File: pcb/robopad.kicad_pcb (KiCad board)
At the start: 2 copper layers, 100 x 100 mm, 34 parts, among them IC1 Left Slider, IC2 Right Slider, SW1 SW_Push, SW2 SW_Push, SW3 SW_Push, SW4 SW_Push, SW5 SW_Push, SW6 SW_Push, SW7 SW_Push, SW8 SW_Push, SW9 SW_Push, U1 XIAO-RP2040-DIP, U2 Left Joystick, U3 Right Joystick, U4 MCP23008-xP, U5 MCP3426Axx-xSN

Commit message: Add branding
Signed-off-by: Urjith Mishra <66270347+TheScientist101@users.noreply.github.com>
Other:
- board text added: "robopad, created by: urjith mishra (thescientist101 on gh)"
- board text removed: "created by: urjith mishra (thescientist101 on gh)"
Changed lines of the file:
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@@
 		(layer "Edge.Cuts")
 	)
-	(gr_text "created by: urjith mishra (thescientist101 on gh)"
-		(at 138.8 148.5 -0)
+	(gr_text "robopad, created by: urjith mishra (thescientist101 on gh)"
+		(at 146.6 148.72 -0)
 		(layer "B.SilkS")
 		(effects
@@
 		)
 	)
-	(gr_text "created by: urjith mishra (thescientist101 on gh)"
-		(at 161.26 148.7 0)
+	(gr_text "robopad, created by: urjith mishra (thescientist101 on gh)"
+		(at 153.4 148.72 0)
 		(layer "F.SilkS")
 		(effects

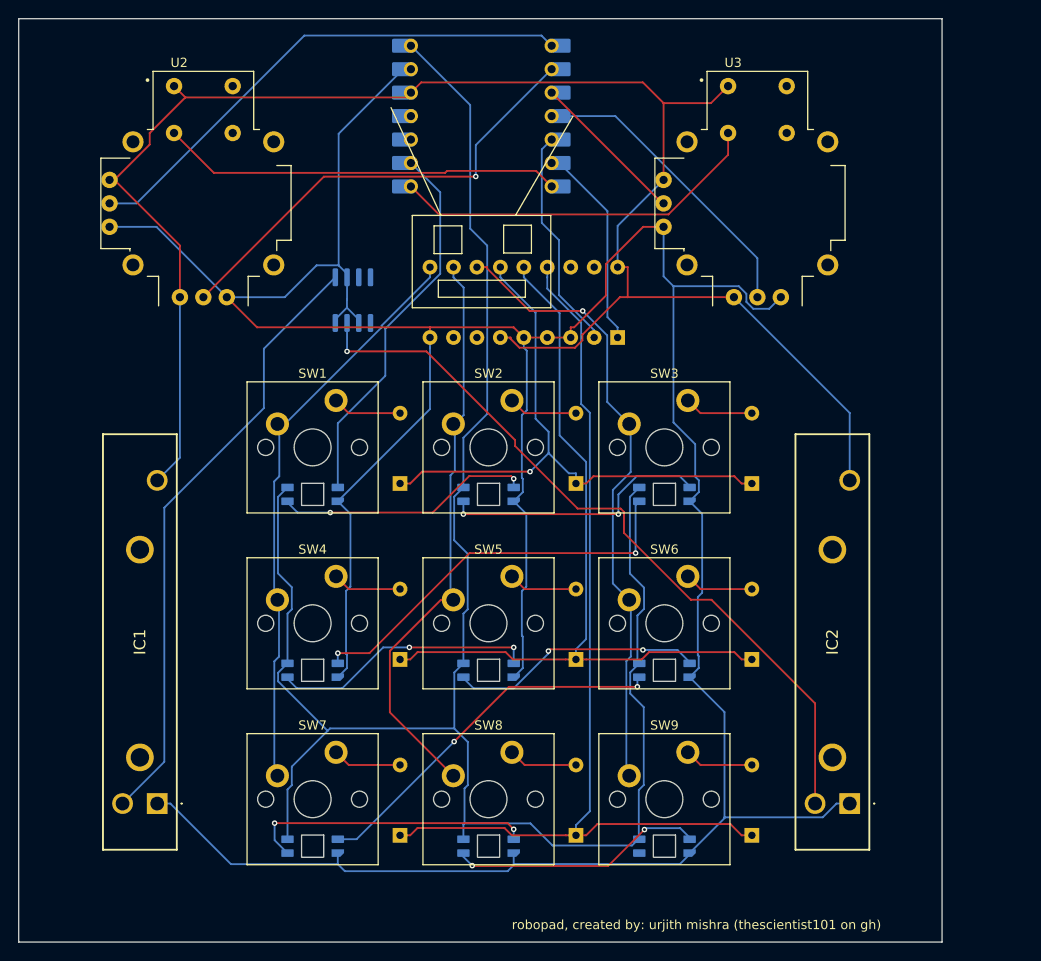
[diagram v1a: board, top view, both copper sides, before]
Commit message: Plug in sda/scl
Signed-off-by: Urjith Mishra <66270347+TheScientist101@users.noreply.github.com>
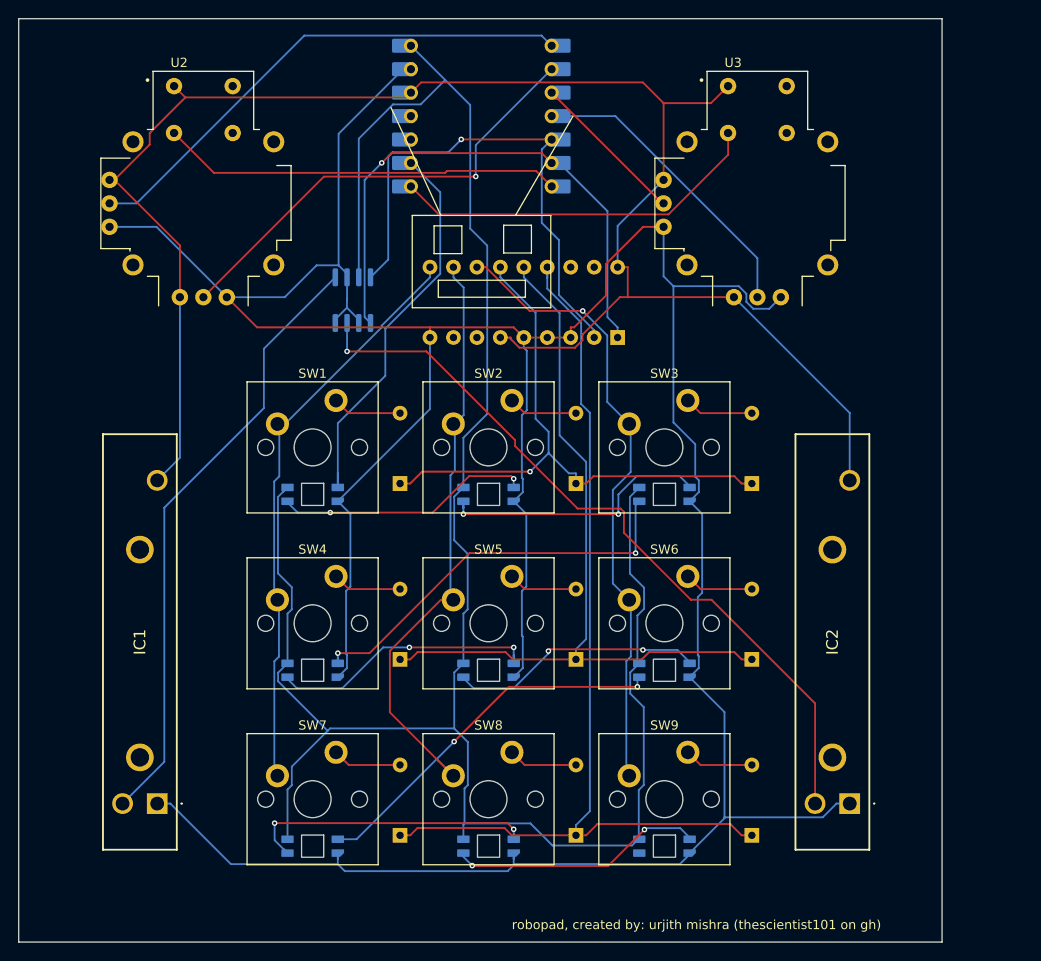
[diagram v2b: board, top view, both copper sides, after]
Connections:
- U5 pad 3: unconnected-(U5-V_{DD}-Pad3) -> +5V
- U5 pad 4: unconnected-(U5-SDA-Pad4) -> sda
- U5 pad 5: unconnected-(U5-SCL-Pad5) -> scl
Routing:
- net scl: track 22.3 -> 60.6 mm, vias 0 -> 1
- net sda: track 25.1 -> 57.8 mm, vias 0 -> 1
- net +5V: track 212.3 -> 240.0 mm
- net col 2: track 62.9 -> 65.8 mm
- net GND: track 368.5 -> 370.3 mm
- net neopixel: track 41.9 -> 43.4 mm
- net col 3: track 67.9 -> 69.3 mm
- net row 3: track 103.8 -> 105.0 mm
- net Net-(LED7-DOUT): track 31.1 -> 32.2 mm
- net Net-(D3-A): track 7.50 -> 8.47 mm
- net Net-(D1-A): track 7.50 -> 8.47 mm
- net Net-(D2-A): track 7.50 -> 8.47 mm
- net Net-(LED4-DOUT): track 28.7 -> 29.6 mm
- net Net-(LED2-DOUT): track 29.4 -> 30.2 mm
- net row 2: track 85.1 -> 85.7 mm
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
